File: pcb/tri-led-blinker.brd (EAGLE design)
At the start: 80 x 49 mm, 13 parts, among them J1 MICRO-USB-SMD(ZX62-B-5PA), K1 TS-1109

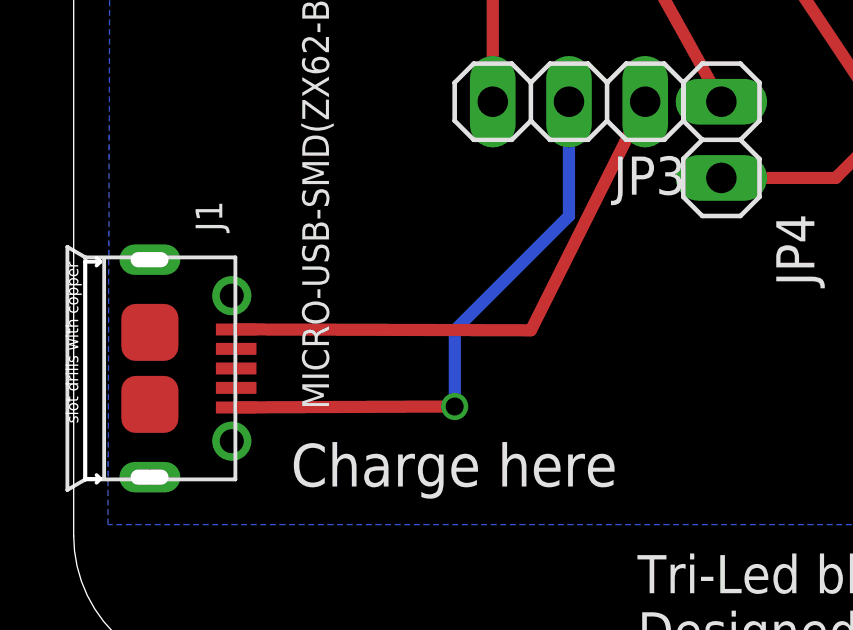
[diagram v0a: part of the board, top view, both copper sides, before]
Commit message: update air wire usb ground
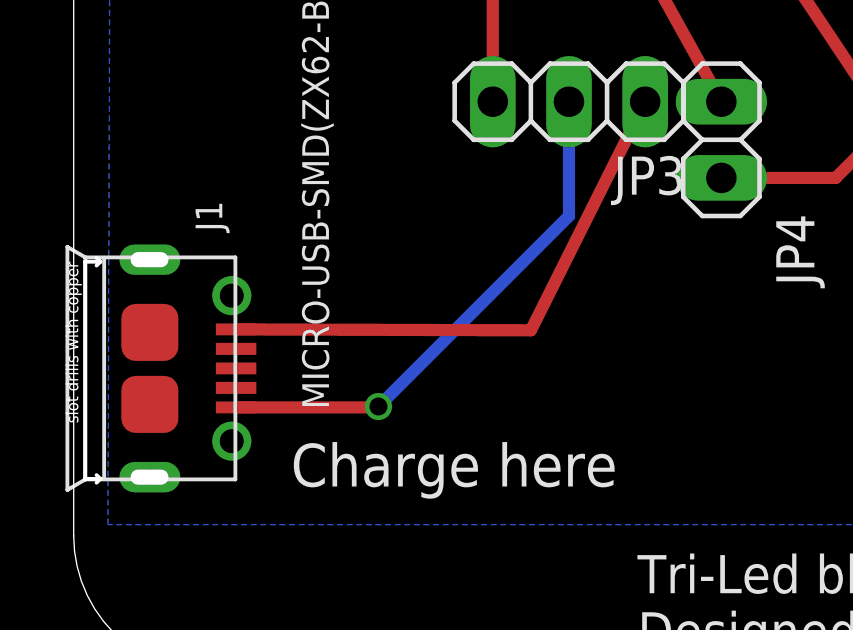
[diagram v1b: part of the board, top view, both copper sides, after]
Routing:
- net GND: track 19.0 -> 17.6 mm
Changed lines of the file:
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@@
 <vertex x="1.143" y="4.953"/>
 </polygon>
-<wire x1="5.415" y1="8.86" x2="12.7" y2="8.89" width="0.4064" layer="1"/>
-<via x="12.7" y="8.89" extent="1-16" drill="0.6" shape="square"/>
-<wire x1="12.7" y1="8.89" x2="12.7" y2="11.43" width="0.4064" layer="16"/>
-<wire x1="12.7" y1="11.43" x2="16.51" y2="15.24" width="0.4064" layer="16"/>
+<wire x1="10.16" y1="8.89" x2="16.51" y2="15.24" width="0.4064" layer="16"/>
 <wire x1="16.51" y1="15.24" x2="16.51" y2="19.05" width="0.4064" layer="16"/>
+<wire x1="5.415" y1="8.86" x2="10.16" y2="8.86" width="0.4064" layer="1"/>
+<wire x1="10.16" y1="8.86" x2="10.16" y2="8.89" width="0.4064" layer="1"/>
+<via x="10.16" y="8.89" extent="1-16" drill="0.6" shape="square"/>
 </signal>
 <signal name="N$1">
